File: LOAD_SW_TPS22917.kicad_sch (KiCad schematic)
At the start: 7 parts, among them U15 TPS22917DBV

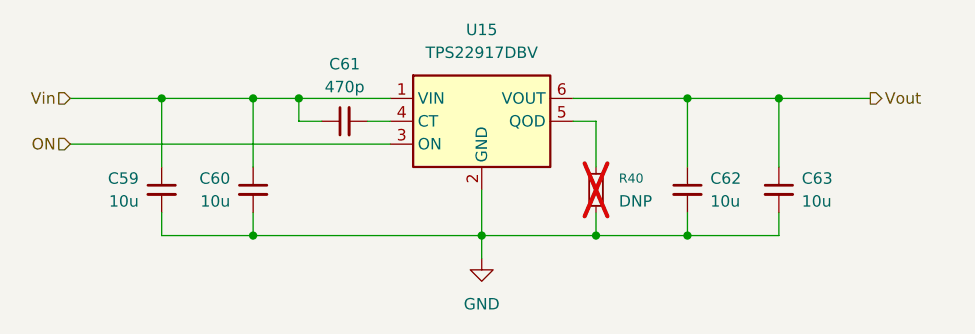
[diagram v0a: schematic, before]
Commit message: Initial layout before routing.
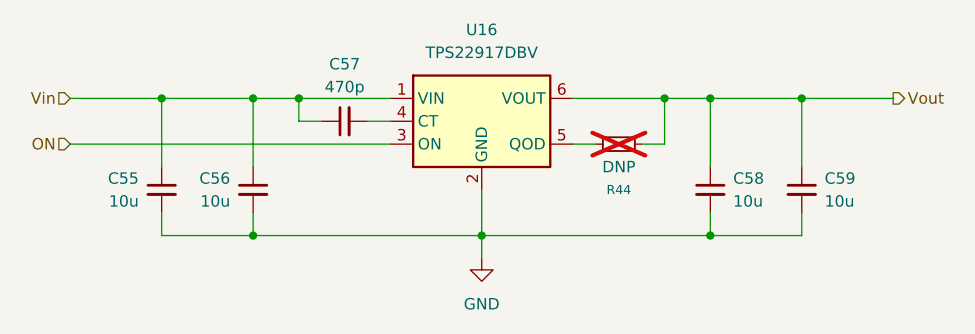
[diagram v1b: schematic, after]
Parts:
- renumbered C59 to C55, C60 to C56, C61 to C57, C62 to C58, C63 to C59, R40 to R44, U15 to U16
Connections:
- net GND: no longer R44.2
- net Vout: now also R44.1
- net at U16.5 (QOD): now also R44.2; no longer R44.1
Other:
- moved on the sheet: C58, C59, R44
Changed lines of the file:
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@@
 	(paper "A4")
 	(junction
-		(at 184.15 97.79)
+		(at 186.69 97.79)
 		(diameter 0)
 		(color 0 0 0 0)
 	)
 	(junction
-		(at 163.83 113.03)
+		(at 171.45 97.79)
 		(diameter 0)
 		(color 0 0 0 0)
 	)
 	(junction
-		(at 173.99 113.03)
+		(at 176.53 113.03)
 		(diameter 0)
 		(color 0 0 0 0)
@@
 	)
 	(junction
-		(at 173.99 97.79)
+		(at 176.53 97.79)
 		(diameter 0)
 		(color 0 0 0 0)
@@
 	(wire
 		(pts
+			(xy 161.29 102.87) (xy 163.83 102.87)
+		)
+		(stroke
+			(width 0)
+			(type default)
+		)
+	)
+	(wire
+		(pts
 			(xy 115.57 105.41) (xy 115.57 97.79)
 		)
@@
 	(wire
 		(pts
-			(xy 184.15 113.03) (xy 184.15 110.49)
+			(xy 186.69 113.03) (xy 186.69 110.49)
 		)
 		(stroke
@@
 	(wire
 		(pts
-			(xy 161.29 97.79) (xy 173.99 97.79)
-		)
-		(stroke
-			(width 0)
-			(type default)
-		)
-	)
-	(wire
-		(pts
-			(xy 163.83 100.33) (xy 163.83 105.41)
-		)
-		(stroke
-			(width 0)
-			(type default)
-		)
-	)
-	(wire
-		(pts
-			(xy 163.83 110.49) (xy 163.83 113.03)
+			(xy 161.29 97.79) (xy 171.45 97.79)
 		)
 		(stroke
@@
 	(wire
 		(pts
-			(xy 161.29 100.33) (xy 163.83 100.33)
-		)
-		(stroke
-			(width 0)
-			(type default)
-		)
-	)
-	(wire
-		(pts
-			(xy 151.13 113.03) (xy 163.83 113.03)
+			(xy 168.91 102.87) (xy 171.45 102.87)
 		)
 		(stroke
@@
 	(wire
 		(pts
-			(xy 163.83 113.03) (xy 173.99 113.03)
-		)
-		(stroke
-			(width 0)
-			(type default)
-		)
-	)
-	(wire
-		(pts
-			(xy 173.99 113.03) (xy 173.99 110.49)
-		)
-		(stroke
-			(width 0)
-			(type default)
-		)
-	)
-	(wire
-		(pts
-			(xy 173.99 97.79) (xy 184.15 97.79)
-		)
-		(stroke
-			(width 0)
-			(type default)
-		)
-	)
-	(wire
-		(pts
-			(xy 184.15 97.79) (xy 194.31 97.79)
+			(xy 171.45 97.79) (xy 171.45 102.87)
+		)
+		(stroke
+			(width 0)
+			(type default)
+		)
+	)
+	(wire
+		(pts
+			(xy 151.13 113.03) (xy 176.53 113.03)
+		)
+		(stroke
+			(width 0)
+			(type default)
+		)
+	)
+	(wire
+		(pts
+			(xy 176.53 113.03) (xy 176.53 110.49)
+		)
+		(stroke
+			(width 0)
+			(type default)
+		)
+	)
+	(wire
+		(pts
+			(xy 176.53 97.79) (xy 186.69 97.79)
+		)
+		(stroke
+			(width 0)
+			(type default)
+		)
+	)
+	(wire
+		(pts
+			(xy 186.69 97.79) (xy 196.85 97.79)
 		)
 		(stroke
@@
 	(wire
 		(pts
-			(xy 173.99 113.03) (xy 184.15 113.03)
+			(xy 176.53 113.03) (xy 186.69 113.03)
 		)
 		(stroke
@@
 	(wire
 		(pts
-			(xy 173.99 97.79) (xy 173.99 105.41)
-		)
-		(stroke
-			(width 0)
-			(type default)
-		)
-	)
-	(wire
-		(pts
-			(xy 184.15 97.79) (xy 184.15 105.41)
+			(xy 171.45 97.79) (xy 176.53 97.79)
+		)
+		(stroke
+			(width 0)
+			(type default)
+		)
+	)
+	(wire
+		(pts
+			(xy 176.53 97.79) (xy 176.53 105.41)
+		)
+		(stroke
+			(width 0)
+			(type default)
+		)
+	)
+	(wire
+		(pts
+			(xy 186.69 97.79) (xy 186.69 105.41)
 		)
 		(stroke
@@
 	(hierarchical_label "Vout"
 		(shape output)
-		(at 194.31 97.79 0)
+		(at 196.85 97.79 0)
 		(effects
 			(font
@@
 	(symbol
 		(lib_id "Device:C_Small")
-		(at 173.99 107.95 0)
+		(at 176.53 107.95 0)
 		(unit 1)
 		(body_style 1)
@@
 		(dnp no)
 		(fields_autoplaced yes)
-		(property "Reference" "C62"
-			(at 176.53 106.6862 0)
+		(property "Reference" "C58"
+			(at 179.07 106.6862 0)
 			(show_name no)
 			(do_not_autoplace no)
@@
 		)
 		(property "Value" "10u"
-			(at 176.53 109.2262 0)
+			(at 179.07 109.2262 0)
 			(show_name no)
 			(do_not_autoplace no)
@@
 		)
 		(property "Footprint" "Capacitor_SMD:C_0603_1608Metric_Pad1.08x0.95mm_HandSolder"
-			(at 173.99 107.95 0)
+			(at 176.53 107.95 0)
 			(hide yes)
 			(show_name no)
@@
 		)
 		(property "Datasheet" ""
-			(at 173.99 107.95 0)
+			(at 176.53 107.95 0)
 			(hide yes)
 			(show_name no)
@@
 		)
 		(property "Description" "Unpolarized capacitor, small symbol"
-			(at 173.99 107.95 0)
+			(at 176.53 107.95 0)
 			(hide yes)
 			(show_name no)
@@
 		(instances
 			(project "DigiFur-Rev1.0"
-				(path "/47dbac06-588f-419b-91d0-b3790df884b4/e25ef6c0-b768-4f2d-b08c-2617d4a733a2"
-					(reference "C62")
-					(unit 1)
-				)
 				(path "/47dbac06-588f-419b-91d0-b3790df884b4/f8199bbe-f54a-440d-afde-f9e5f212ef78"
-					(reference "C67")
+					(reference "C58")
 					(unit 1)
 				)
@@
 		(in_pos_files yes)
 		(dnp no)
-		(property "Reference" "C60"
+		(property "Reference" "C56"
 			(at 123.19 106.6862 0)
 			(show_name no)
@@
 		(instances
 			(project "DigiFur-Rev1.0"
-				(path "/47dbac06-588f-419b-91d0-b3790df884b4/e25ef6c0-b768-4f2d-b08c-2617d4a733a2"
-					(reference "C60")
-					(unit 1)
-				)
 				(path "/47dbac06-588f-419b-91d0-b3790df884b4/f8199bbe-f54a-440d-afde-f9e5f212ef78"
-					(reference "C65")
+					(reference "C56")
 					(unit 1)
 				)
@@
 		(dnp no)
 		(fields_autoplaced yes)
-		(property "Reference" "#PWR063"
+		(property "Reference" "#PWR064"
 			(at 151.13 121.92 0)
 			(hide yes)
@@
 		(instances
 			(project "DigiFur-Rev1.0"
-				(path "/47dbac06-588f-419b-91d0-b3790df884b4/e25ef6c0-b768-4f2d-b08c-2617d4a733a2"
-					(reference "#PWR063")
-					(unit 1)
-				)
 				(path "/47dbac06-588f-419b-91d0-b3790df884b4/f8199bbe-f54a-440d-afde-f9e5f212ef78"
 					(reference "#PWR064")
@@
 	(symbol
 		(lib_id "Device:R_Small")
-		(at 163.83 107.95 0)
+		(at 166.37 102.87 270)
 		(unit 1)
 		(body_style 1)
@@
 		(in_pos_files yes)
 		(dnp yes)
-		(fields_autoplaced yes)
-		(property "Reference" "R40"
-			(at 166.37 106.6799 0)
+		(property "Reference" "R44"
+			(at 166.37 107.95 90)
 			(show_name no)
 			(do_not_autoplace no)
@@
 					(size 1.016 1.016)
 				)
-				(justify left)
 			)
 		)
 		(property "Value" "DNP"
-			(at 166.37 109.2199 0)
-			(show_name no)
-			(do_not_autoplace no)
-			(effects
-				(font
-					(size 1.27 1.27)
-				)
-				(justify left)
+			(at 166.37 105.41 90)
+			(show_name no)
+			(do_not_autoplace no)
+			(effects
+				(font
+					(size 1.27 1.27)
+				)
 			)
 		)
 		(property "Footprint" "Resistor_SMD:R_0603_1608Metric_Pad0.98x0.95mm_HandSolder"
-			(at 163.83 107.95 0)
+			(at 166.37 102.87 0)
 			(hide yes)
 			(show_name no)
@@
 		)
 		(property "Datasheet" ""
-			(at 163.83 107.95 0)
+			(at 166.37 102.87 0)
 			(hide yes)
 			(show_name no)
@@
 		)
 		(property "Description" "Resistor, small symbol"
-			(at 163.83 107.95 0)
+			(at 166.37 102.87 0)
 			(hide yes)
 			(show_name no)
@@
 		(instances
 			(project "DigiFur-Rev1.0"
-				(path "/47dbac06-588f-419b-91d0-b3790df884b4/e25ef6c0-b768-4f2d-b08c-2617d4a733a2"
-					(reference "R40")
-					(unit 1)
-				)
 				(path "/47dbac06-588f-419b-91d0-b3790df884b4/f8199bbe-f54a-440d-afde-f9e5f212ef78"
-					(reference "R41")
+					(reference "R44")
 					(unit 1)
 				)
@@
 		(in_pos_files yes)
 		(dnp no)
-		(property "Reference" "C59"
+		(property "Reference" "C55"
 			(at 113.03 106.6862 0)
 			(show_name no)
@@
 		(instances
 			(project "DigiFur-Rev1.0"
-				(path "/47dbac06-588f-419b-91d0-b3790df884b4/e25ef6c0-b768-4f2d-b08c-2617d4a733a2"
-					(reference "C59")
-					(unit 1)
-				)
 				(path "/47dbac06-588f-419b-91d0-b3790df884b4/f8199bbe-f54a-440d-afde-f9e5f212ef78"
-					(reference "C64")
+					(reference "C55")
 					(unit 1)
 				)
@@
 	(symbol
 		(lib_id "Device:C_Small")
-		(at 184.15 107.95 0)
+		(at 186.69 107.95 0)
 		(unit 1)
 		(body_style 1)
@@
 		(dnp no)
 		(fields_autoplaced yes)
-		(property "Reference" "C63"
-			(at 186.69 106.6862 0)
+		(property "Reference" "C59"
+			(at 189.23 106.6862 0)
 			(show_name no)
 			(do_not_autoplace no)
@@
 		)
 		(property "Value" "10u"
-			(at 186.69 109.2262 0)
+			(at 189.23 109.2262 0)
 			(show_name no)
 			(do_not_autoplace no)
@@
 		)
 		(property "Footprint" "Capacitor_SMD:C_0603_1608Metric_Pad1.08x0.95mm_HandSolder"
-			(at 184.15 107.95 0)
+			(at 186.69 107.95 0)
 			(hide yes)
 			(show_name no)
@@
 		)
 		(property "Datasheet" ""
-			(at 184.15 107.95 0)
+			(at 186.69 107.95 0)
 			(hide yes)
 			(show_name no)
@@
 		)
 		(property "Description" "Unpolarized capacitor, small symbol"
-			(at 184.15 107.95 0)
+			(at 186.69 107.95 0)
 			(hide yes)
 			(show_name no)
@@
 		(instances
 			(project "DigiFur-Rev1.0"
-				(path "/47dbac06-588f-419b-91d0-b3790df884b4/e25ef6c0-b768-4f2d-b08c-2617d4a733a2"
-					(reference "C63")
-					(unit 1)
-				)
 				(path "/47dbac06-588f-419b-91d0-b3790df884b4/f8199bbe-f54a-440d-afde-f9e5f212ef78"
-					(reference "C68")
+					(reference "C59")
 					(unit 1)
 				)
@@
 		(dnp no)
 		(fields_autoplaced yes)
-		(property "Reference" "C61"
+		(property "Reference" "C57"
 			(at 135.8963 93.98 90)
 			(show_name no)
@@
 		(instances
 			(project "DigiFur-Rev1.0"
-				(path "/47dbac06-588f-419b-91d0-b3790df884b4/e25ef6c0-b768-4f2d-b08c-2617d4a733a2"
-					(reference "C61")
-					(unit 1)
-				)
 				(path "/47dbac06-588f-419b-91d0-b3790df884b4/f8199bbe-f54a-440d-afde-f9e5f212ef78"
-					(reference "C66")
+					(reference "C57")
 					(unit 1)
 				)
@@
 		(dnp no)
 		(fields_autoplaced yes)
-		(property "Reference" "U15"
+		(property "Reference" "U16"
 			(at 151.13 90.17 0)
 			(show_name no)
@@
 		(instances
 			(project "DigiFur-Rev1.0"
-				(path "/47dbac06-588f-419b-91d0-b3790df884b4/e25ef6c0-b768-4f2d-b08c-2617d4a733a2"
-					(reference "U15")
-					(unit 1)
-				)
 				(path "/47dbac06-588f-419b-91d0-b3790df884b4/f8199bbe-f54a-440d-afde-f9e5f212ef78"
 					(reference "U16")

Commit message: PCB layout done, signal routing finished, power routing remaining.
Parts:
- renumbered R44 to R45
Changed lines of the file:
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@@
 		(dnp no)
 		(fields_autoplaced yes)
-		(property "Reference" "#PWR064"
+		(property "Reference" "#PWR065"
 			(at 151.13 121.92 0)
 			(hide yes)
@@
 			(project "DigiFur-Rev1.0"
 				(path "/47dbac06-588f-419b-91d0-b3790df884b4/f8199bbe-f54a-440d-afde-f9e5f212ef78"
-					(reference "#PWR064")
+					(reference "#PWR065")
 					(unit 1)
 				)
@@
 		(in_pos_files yes)
 		(dnp yes)
-		(property "Reference" "R44"
+		(property "Reference" "R45"
 			(at 166.37 107.95 90)
 			(show_name no)
@@
 			(project "DigiFur-Rev1.0"
 				(path "/47dbac06-588f-419b-91d0-b3790df884b4/f8199bbe-f54a-440d-afde-f9e5f212ef78"
-					(reference "R44")
+					(reference "R45")
 					(unit 1)
 				)

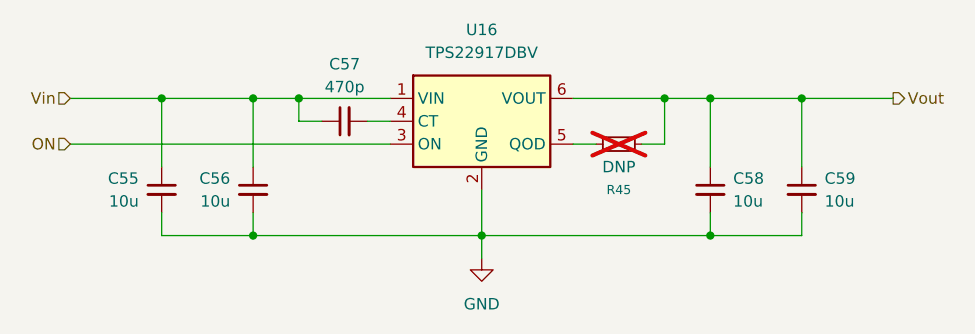
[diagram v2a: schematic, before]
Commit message: Revision to fix problems from first board fab
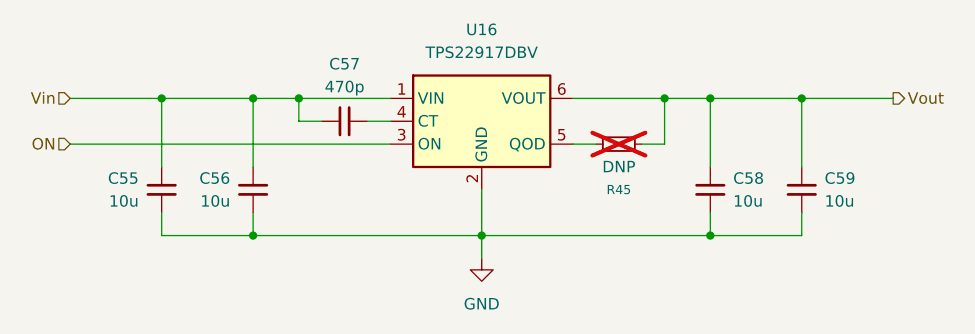
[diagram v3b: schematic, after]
